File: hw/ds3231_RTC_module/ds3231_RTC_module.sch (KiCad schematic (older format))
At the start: 23 parts, among them J101 Conn_01x07, Q2101 AO3401A, Q2102 DMG1013T, U2101 DS3231M, U2102 CAT24C256, U2103 DS3231MZ

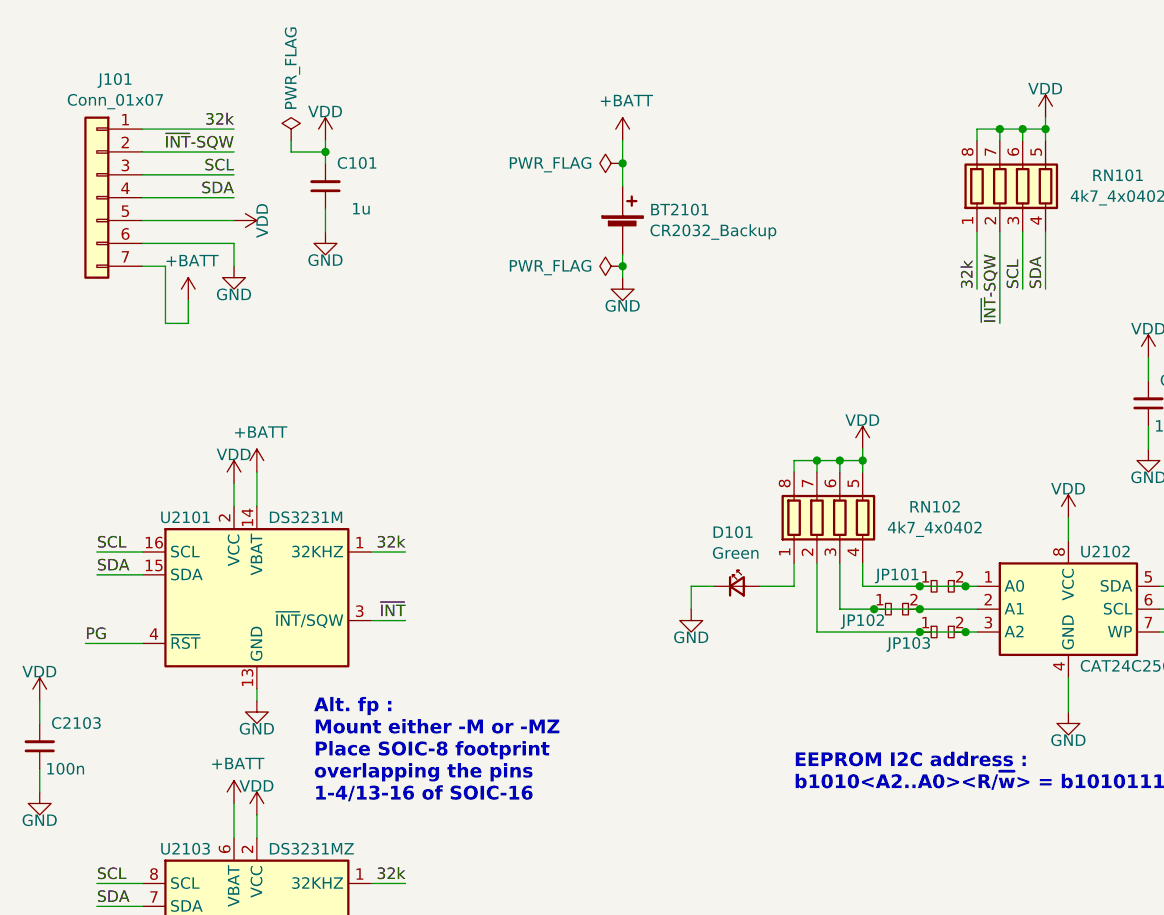
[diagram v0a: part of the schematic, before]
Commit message: Quick 1st layout & route of the RTC sub-module
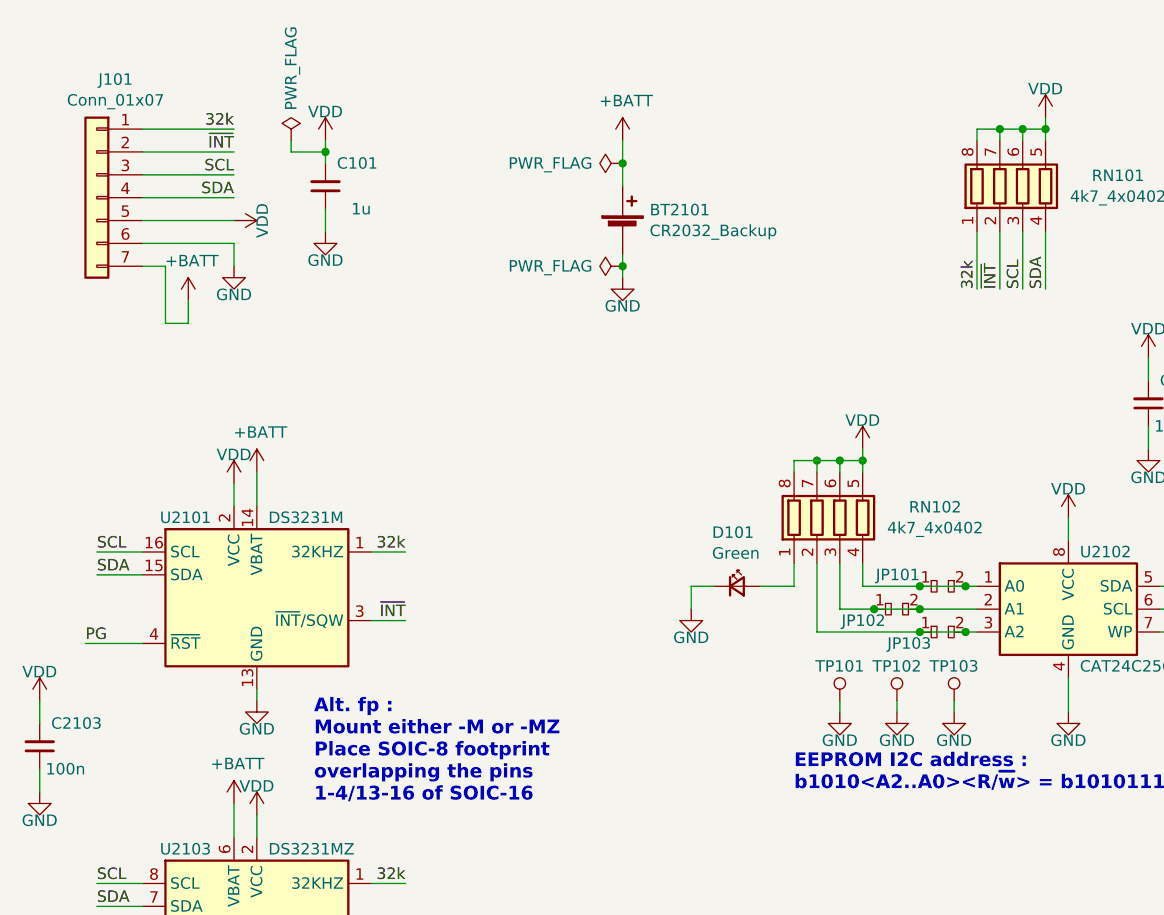
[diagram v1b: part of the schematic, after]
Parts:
- added TP101, TP102, TP103: TP, customlib_mj_fp:TP_SMD_1.2c, symbol customlib_mj:TP
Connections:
- net ~INT~-SQW is gone; now on net ~INT~: J101.2 (Pin_2), RN101.2 (R2.1)
- net GND: now also TP101.1, TP102.1, TP103.1
